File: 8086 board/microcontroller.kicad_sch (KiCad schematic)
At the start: 24 parts, among them J2 USB, U20 ATmega328P, U21 74HC595, U22 74HC595, U23 74HC595, U24 74HC165, U25 74HC165, U26 CH340C, Y1 16MHz

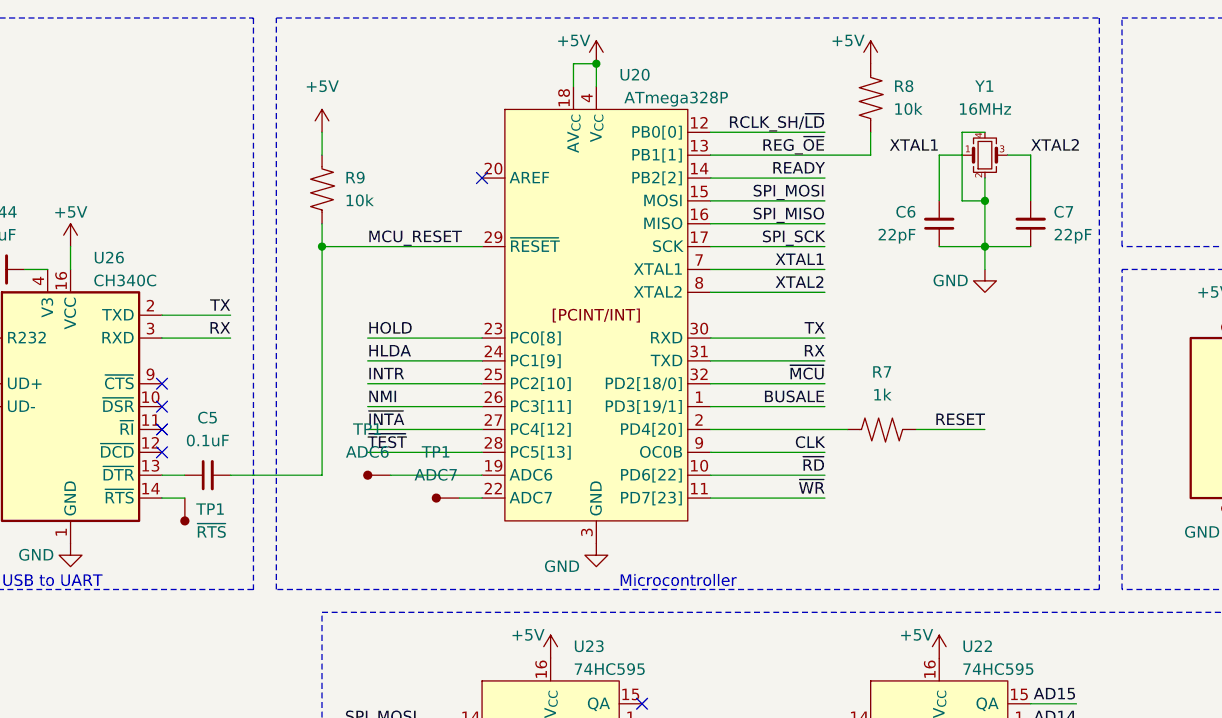
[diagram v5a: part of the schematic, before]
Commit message: small schematic  changes to better fit PCB
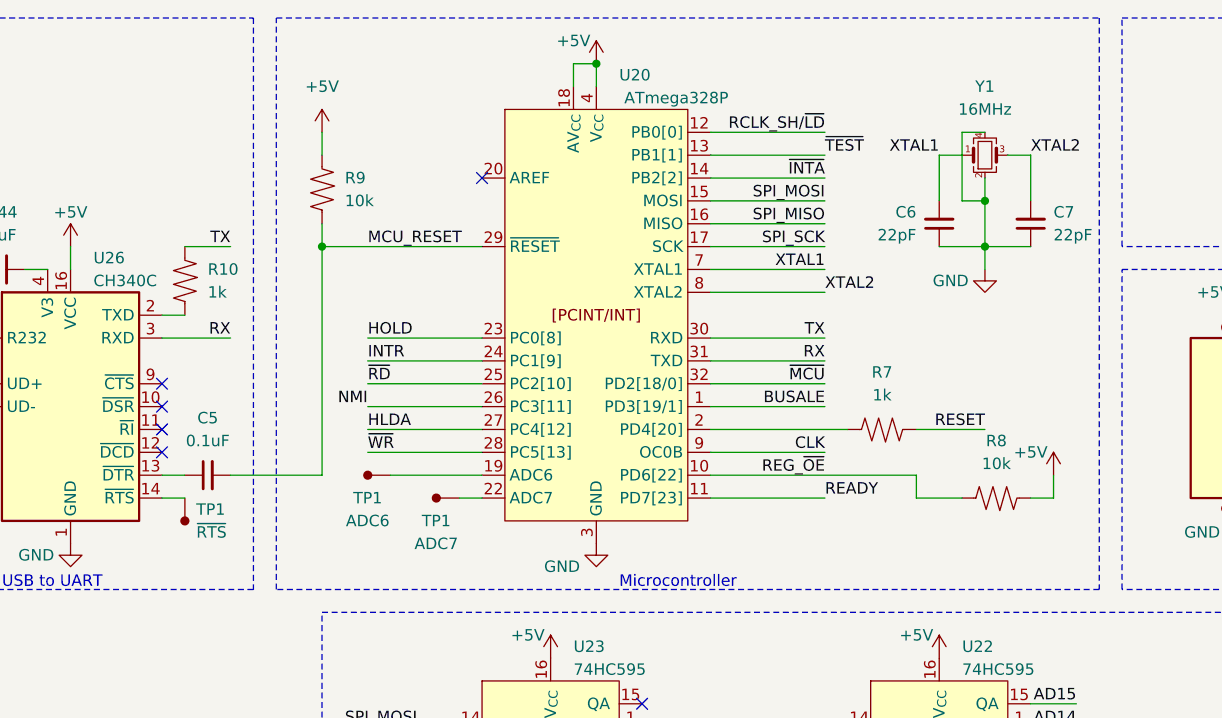
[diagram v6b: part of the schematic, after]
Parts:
- added R10: 1k, Resistor_SMD:R_0603_1608Metric_Pad0.98x0.95mm_HandSolder, symbol 8086PC:R
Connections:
- net HLDA: now also U20.27 (PC4[12]); no longer U20.24 (PC1[9])
- net INTR: now also U20.24 (PC1[9]); no longer U20.25 (PC2[10])
- net READY: now also U20.11 (PD7[23]); no longer U20.14 (PB2[2])
- net REG_~{OE}: now also U20.10 (PD6[22]); no longer U20.13 (PB1[1])
- net TX: now also R10.2; no longer U26.2 (TXD)
- net ~{INTA}: now also U20.14 (PB2[2]); no longer U20.27 (PC4[12])
- net ~{RD}: now also U20.25 (PC2[10]); no longer U20.10 (PD6[22])
- net ~{TEST}: now also U20.13 (PB1[1]); no longer U20.28 (PC5[13])
- net ~{WR}: now also U20.28 (PC5[13]); no longer U20.11 (PD7[23])
- new net: R10.1, U26.2 (TXD)
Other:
- moved on the sheet: R8

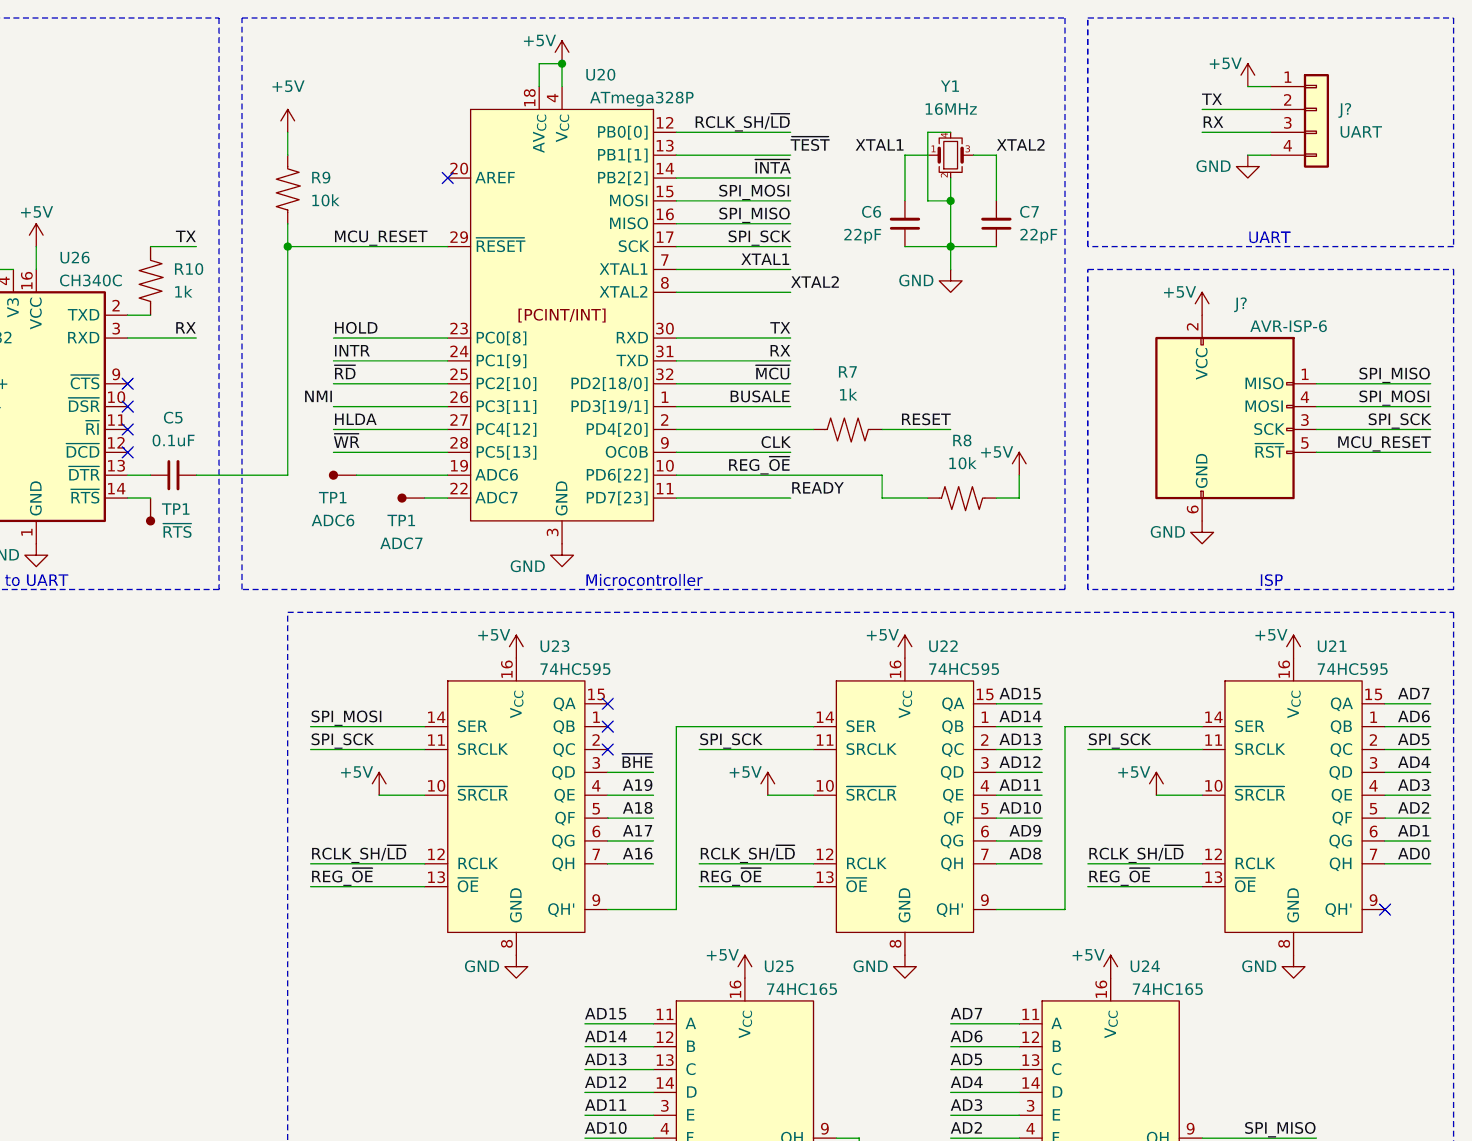
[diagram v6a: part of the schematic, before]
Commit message: schematic: fix LCD RD bug, geographical reannotation
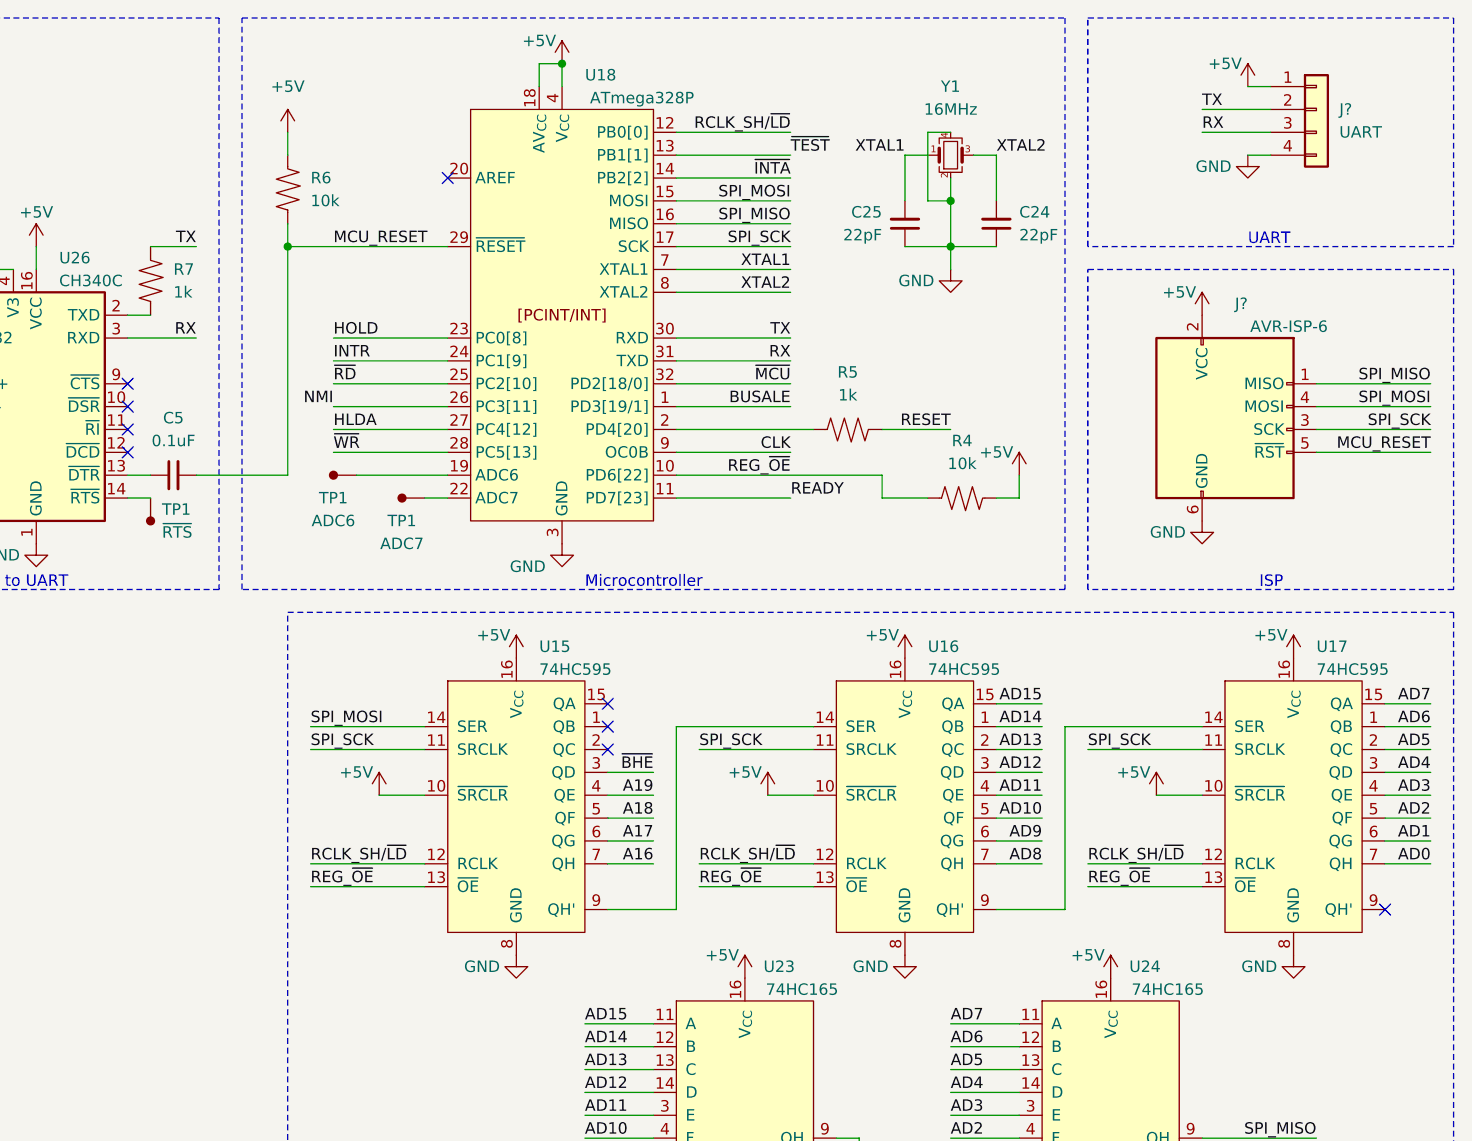
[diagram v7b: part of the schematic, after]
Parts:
- TP1: value ADC6 -> ~; Signal (none) -> ADC6; now left out of the parts list
- TP1: value ~{RTS} -> ~; Signal (none) -> ~{RTS}; now left out of the parts list
- TP1: value ADC7 -> ~; Signal (none) -> ADC7; now left out of the parts list
- renumbered C7 to C24, C6 to C25, R8 to R4, R7 to R5, R9 to R6, R10 to R7, U23 to U15, U22 to U16, U21 to U17, U20 to U18, U25 to U23
